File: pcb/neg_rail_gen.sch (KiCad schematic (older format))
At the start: 24 parts, among them U5 LM2596S-ADJ

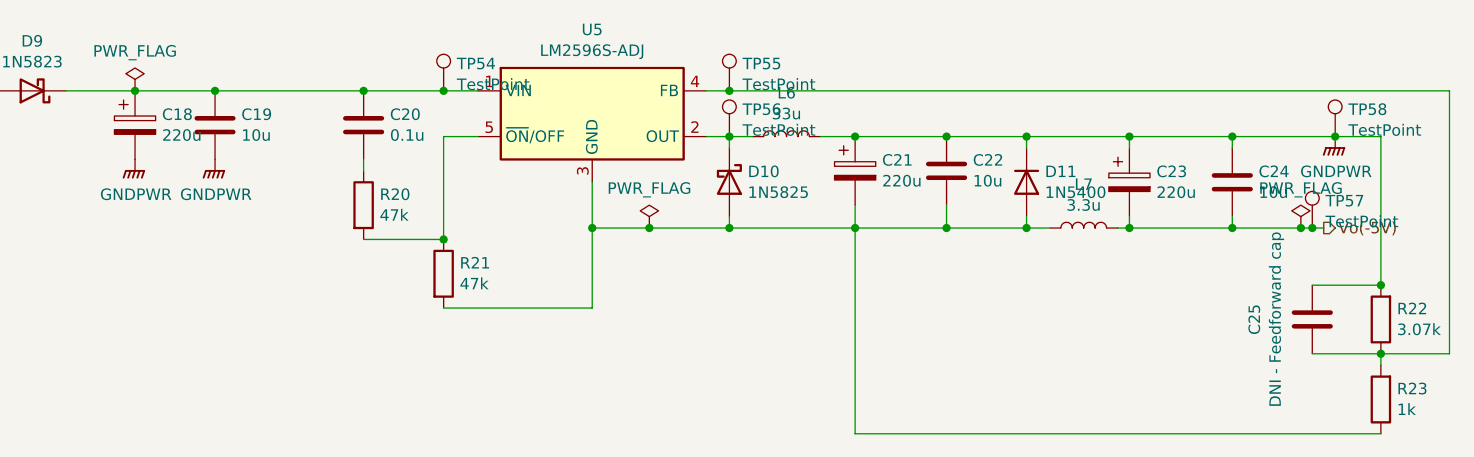
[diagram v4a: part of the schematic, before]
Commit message: Update footprints, move to 0603 passives for JLCPCB assembly, create transformer footprints
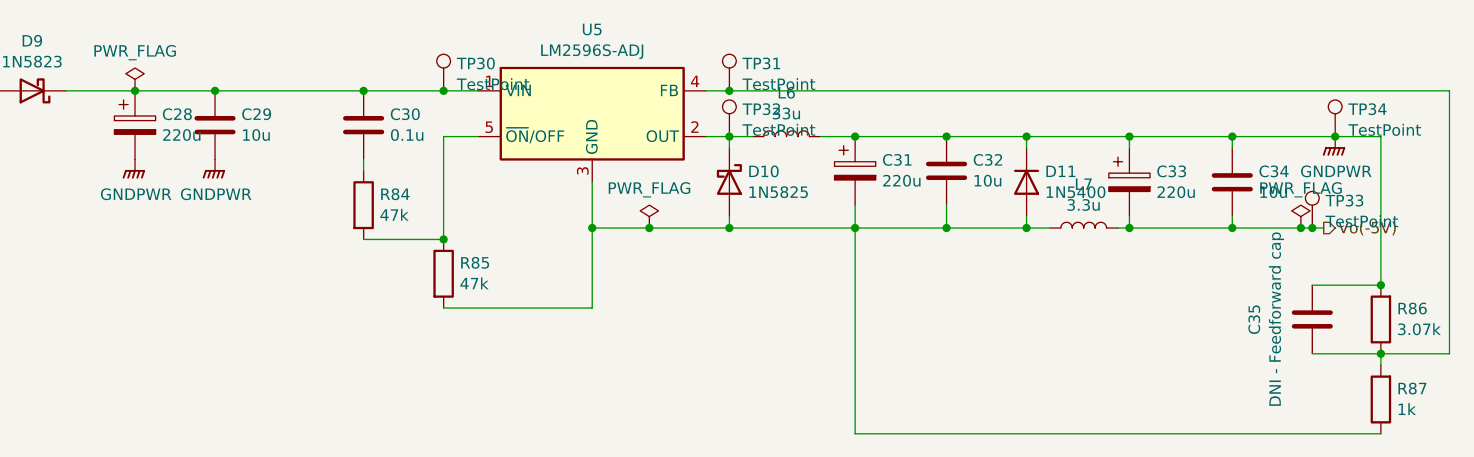
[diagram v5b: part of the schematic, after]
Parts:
- C29: renamed from C19; footprint Capacitor_SMD:C_0805_2012Metric_Pad1.15x1.40mm_HandSolder -> Capacitor_SMD:C_0603_1608Metric
- C30: renamed from C20; footprint Capacitor_SMD:C_0805_2012Metric_Pad1.15x1.40mm_HandSolder -> Capacitor_SMD:C_0603_1608Metric
- C32: renamed from C22; footprint Capacitor_SMD:C_0805_2012Metric_Pad1.15x1.40mm_HandSolder -> Capacitor_SMD:C_0603_1608Metric
- C34: renamed from C24; footprint Capacitor_SMD:C_0805_2012Metric_Pad1.15x1.40mm_HandSolder -> Capacitor_SMD:C_0603_1608Metric
- L6: footprint (none) -> Inductor_SMD:L_Bourns_SRR1260
- L7: footprint (none) -> Inductor_THT:L_Axial_L9.5mm_D4.0mm_P12.70mm_Horizontal_Fastron_SMCC
- R84: renamed from R20; footprint Resistor_SMD:R_0805_2012Metric_Pad1.20x1.40mm_HandSolder -> Resistor_SMD:R_0603_1608Metric
- R85: renamed from R21; footprint Resistor_SMD:R_0805_2012Metric_Pad1.20x1.40mm_HandSolder -> Resistor_SMD:R_0603_1608Metric
- R86: renamed from R22; footprint Resistor_SMD:R_0805_2012Metric_Pad1.20x1.40mm_HandSolder -> Resistor_SMD:R_0603_1608Metric
- R87: renamed from R23; footprint Resistor_SMD:R_0805_2012Metric_Pad1.20x1.40mm_HandSolder -> Resistor_SMD:R_0603_1608Metric
- TP30: renamed from TP54; footprint (none) -> TestPoint:TestPoint_Pad_D1.5mm
- TP31: renamed from TP55; footprint (none) -> TestPoint:TestPoint_Pad_D1.5mm
- TP32: renamed from TP56; footprint (none) -> TestPoint:TestPoint_Pad_D1.5mm
- TP33: renamed from TP57; footprint (none) -> TestPoint:TestPoint_Pad_D1.5mm
- TP34: renamed from TP58; footprint (none) -> TestPoint:TestPoint_Pad_D1.5mm
- renumbered C18 to C28, C21 to C31, C23 to C33, C25 to C35
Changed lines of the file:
@@
 F 0 "L6" V 6840 3600 50  0000 C CNN
 F 1 "33u" V 6749 3600 50  0000 C CNN
-F 2 "" H 6650 3600 50  0001 C CNN
+F 2 "Inductor_SMD:L_Bourns_SRR1260" H 6650 3600 50  0001 C CNN
 F 3 "~" H 6650 3600 50  0001 C CNN
 	1    6650 3600
@@
 	6300 3600 6400 3600
 $Comp
-L Device:CP C21
+L Device:CP C31
 U 1 1 5FD71007
 P 6950 3750
-F 0 "C21" H 7068 3796 50  0000 L CNN
+F 0 "C31" H 7068 3796 50  0000 L CNN
 F 1 "220u" H 7068 3705 50  0000 L CNN
 F 2 "Capacitor_Tantalum_SMD:CP_EIA-7343-20_Kemet-V_Pad2.25x2.55mm_HandSolder" H 6988 3600 50  0001 C CNN
@@
 $EndComp
 $Comp
-L Device:C C22
+L Device:C C32
 U 1 1 5FD73530
 P 7350 3750
-F 0 "C22" H 7235 3704 50  0000 R CNN
+F 0 "C32" H 7235 3704 50  0000 R CNN
 F 1 "10u" H 7235 3795 50  0000 R CNN
-F 2 "Capacitor_SMD:C_0805_2012Metric_Pad1.15x1.40mm_HandSolder" H 7388 3600 50  0001 C CNN
+F 2 "Capacitor_SMD:C_0603_1608Metric" H 7388 3600 50  0001 C CNN
 F 3 "~" H 7350 3750 50  0001 C CNN
 	1    7350 3750
@@
 F 0 "L7" V 8140 4000 50  0000 C CNN
 F 1 "3.3u" V 8049 4000 50  0000 C CNN
-F 2 "" H 7950 4000 50  0001 C CNN
+F 2 "Inductor_THT:L_Axial_L9.5mm_D4.0mm_P12.70mm_Horizontal_Fastron_SMCC" H 7950 4000 50  0001 C CNN
 F 3 "~" H 7950 4000 50  0001 C CNN
 	1    7950 4000
@@
 Connection ~ 8150 3600
 $Comp
-L Device:C C24
+L Device:C C34
 U 1 1 5FD79EE0
 P 8600 3800
-F 0 "C24" H 8485 3754 50  0000 R CNN
+F 0 "C34" H 8485 3754 50  0000 R CNN
 F 1 "10u" H 8485 3845 50  0000 R CNN
-F 2 "Capacitor_SMD:C_0805_2012Metric_Pad1.15x1.40mm_HandSolder" H 8638 3650 50  0001 C CNN
+F 2 "Capacitor_SMD:C_0603_1608Metric" H 8638 3650 50  0001 C CNN
 F 3 "~" H 8600 3800 50  0001 C CNN
 	1    8600 3800
@@
 	6400 3600 6500 3600
 $Comp
-L Device:CP C18
+L Device:CP C28
 U 1 1 5FD8CD2C
 P 3800 3550
-F 0 "C18" H 3918 3596 50  0000 L CNN
+F 0 "C28" H 3918 3596 50  0000 L CNN
 F 1 "220u" H 3918 3505 50  0000 L CNN
 F 2 "Capacitor_Tantalum_SMD:CP_EIA-7343-20_Kemet-V_Pad2.25x2.55mm_HandSolder" H 3838 3400 50  0001 C CNN
@@
 $EndComp
 $Comp
-L power:GNDPWR #PWR0139
+L power:GNDPWR #PWR069
 U 1 1 5FD8CD32
 P 4150 3700
-F 0 "#PWR0139" H 4150 3500 50  0001 C CNN
+F 0 "#PWR069" H 4150 3500 50  0001 C CNN
 F 1 "GNDPWR" H 4154 3546 50  0000 C CNN
 F 2 "" H 4150 3650 50  0001 C CNN
@@
 $EndComp
 $Comp
-L power:GNDPWR #PWR0140
+L power:GNDPWR #PWR068
 U 1 1 5FD8CD38
 P 3800 3700
-F 0 "#PWR0140" H 3800 3500 50  0001 C CNN
+F 0 "#PWR068" H 3800 3500 50  0001 C CNN
 F 1 "GNDPWR" H 3804 3546 50  0000 C CNN
 F 2 "" H 3800 3650 50  0001 C CNN
@@
 $EndComp
 $Comp
-L Device:C C19
+L Device:C C29
 U 1 1 5FD8CD3E
 P 4150 3550
-F 0 "C19" H 4265 3596 50  0000 L CNN
+F 0 "C29" H 4265 3596 50  0000 L CNN
 F 1 "10u" H 4265 3505 50  0000 L CNN
-F 2 "Capacitor_SMD:C_0805_2012Metric_Pad1.15x1.40mm_HandSolder" H 4188 3400 50  0001 C CNN
+F 2 "Capacitor_SMD:C_0603_1608Metric" H 4188 3400 50  0001 C CNN
 F 3 "~" H 4150 3550 50  0001 C CNN
 	1    4150 3550
@@
 Connection ~ 8600 4000
 $Comp
-L Device:CP C23
+L Device:CP C33
 U 1 1 5FDC37D7
 P 8150 3800
-F 0 "C23" H 8268 3846 50  0000 L CNN
+F 0 "C33" H 8268 3846 50  0000 L CNN
 F 1 "220u" H 8268 3755 50  0000 L CNN
 F 2 "Capacitor_Tantalum_SMD:CP_EIA-7343-20_Kemet-V_Pad2.25x2.55mm_HandSolder" H 8188 3650 50  0001 C CNN
@@
 	8100 4000 8150 4000
 $Comp
-L power:GNDPWR #PWR0141
+L power:GNDPWR #PWR070
 U 1 1 5FDC93D0
 P 9050 3600
-F 0 "#PWR0141" H 9050 3400 50  0001 C CNN
+F 0 "#PWR070" H 9050 3400 50  0001 C CNN
 F 1 "GNDPWR" H 9054 3446 50  0000 C CNN
 F 2 "" H 9050 3550 50  0001 C CNN
@@
 	7700 4000 7800 4000
 $Comp
-L Device:R R21
+L Device:R R85
 U 1 1 5FDDC2C2
 P 5150 4200
-F 0 "R21" H 5220 4246 50  0000 L CNN
+F 0 "R85" H 5220 4246 50  0000 L CNN
 F 1 "47k" H 5220 4155 50  0000 L CNN
-F 2 "Resistor_SMD:R_0805_2012Metric_Pad1.20x1.40mm_HandSolder" V 5080 4200 50  0001 C CNN
+F 2 "Resistor_SMD:R_0603_1608Metric" V 5080 4200 50  0001 C CNN
 F 3 "~" H 5150 4200 50  0001 C CNN
 	1    5150 4200
@@
 $EndComp
 $Comp
-L Device:R R20
+L Device:R R84
 U 1 1 5FDDC644
 P 4800 3900
-F 0 "R20" H 4870 3946 50  0000 L CNN
+F 0 "R84" H 4870 3946 50  0000 L CNN
 F 1 "47k" H 4870 3855 50  0000 L CNN
-F 2 "Resistor_SMD:R_0805_2012Metric_Pad1.20x1.40mm_HandSolder" V 4730 3900 50  0001 C CNN
+F 2 "Resistor_SMD:R_0603_1608Metric" V 4730 3900 50  0001 C CNN
 F 3 "~" H 4800 3900 50  0001 C CNN
 	1    4800 3900
@@
 Connection ~ 5800 4000
 $Comp
-L Device:C C20
+L Device:C C30
 U 1 1 5FDEA8C9
 P 4800 3550
-F 0 "C20" H 4915 3596 50  0000 L CNN
+F 0 "C30" H 4915 3596 50  0000 L CNN
 F 1 "0.1u" H 4915 3505 50  0000 L CNN
-F 2 "Capacitor_SMD:C_0805_2012Metric_Pad1.15x1.40mm_HandSolder" H 4838 3400 50  0001 C CNN
+F 2 "Capacitor_SMD:C_0603_1608Metric" H 4838 3400 50  0001 C CNN
 F 3 "~" H 4800 3550 50  0001 C CNN
 	1    4800 3550
@@
 	6950 3600 7350 3600
 $Comp
-L Device:C C25
+L Device:C C35
 U 1 1 5FE0D49B
 P 8950 4400
-F 0 "C25" V 9202 4400 50  0000 C CNN
+F 0 "C35" V 9202 4400 50  0000 C CNN
 F 1 "DNI - Feedforward cap" V 9111 4400 50  0000 C CNN
 F 2 "Capacitor_SMD:C_0805_2012Metric_Pad1.15x1.40mm_HandSolder" H 8988 4250 50  0001 C CNN
@@
 $EndComp
 $Comp
-L Device:R R22
+L Device:R R86
 U 1 1 5FE19832
 P 9250 4400
-F 0 "R22" H 9180 4354 50  0000 R CNN
+F 0 "R86" H 9180 4354 50  0000 R CNN
 F 1 "3.07k" H 9180 4445 50  0000 R CNN
-F 2 "Resistor_SMD:R_0805_2012Metric_Pad1.20x1.40mm_HandSolder" V 9180 4400 50  0001 C CNN
+F 2 "Resistor_SMD:R_0603_1608Metric" V 9180 4400 50  0001 C CNN
 F 3 "~" H 9250 4400 50  0001 C CNN
 	1    9250 4400
@@
 	6950 4900 9250 4900
 $Comp
-L Device:R R23
+L Device:R R87
 U 1 1 5FE1B1CA
 P 9250 4750
-F 0 "R23" H 9180 4704 50  0000 R CNN
+F 0 "R87" H 9180 4704 50  0000 R CNN
 F 1 "1k" H 9180 4795 50  0000 R CNN
-F 2 "Resistor_SMD:R_0805_2012Metric_Pad1.20x1.40mm_HandSolder" V 9180 4750 50  0001 C CNN
+F 2 "Resistor_SMD:R_0603_1608Metric" V 9180 4750 50  0001 C CNN
 F 3 "~" H 9250 4750 50  0001 C CNN
 	1    9250 4750
@@
 	8950 4550 9250 4550
 $Comp
-L power:PWR_FLAG #FLG0102
+L power:PWR_FLAG #FLG07
 U 1 1 5FE36453
 P 8900 4000
-F 0 "#FLG0102" H 8900 4075 50  0001 C CNN
+F 0 "#FLG07" H 8900 4075 50  0001 C CNN
 F 1 "PWR_FLAG" H 8900 4173 50  0000 C CNN
 F 2 "" H 8900 4000 50  0001 C CNN
@@
 	2450 3400 2750 3400
 $Comp
-L power:PWR_FLAG #FLG0104
+L power:PWR_FLAG #FLG05
 U 1 1 5FE3E0B5
 P 3800 3400
-F 0 "#FLG0104" H 3800 3475 50  0001 C CNN
+F 0 "#FLG05" H 3800 3475 50  0001 C CNN
 F 1 "PWR_FLAG" H 3800 3573 50  0000 C CNN
 F 2 "" H 3800 3400 50  0001 C CNN
@@
 $EndComp
 $Comp
-L power:PWR_FLAG #FLG0105
+L power:PWR_FLAG #FLG06
 U 1 1 5FE3F4DD
 P 6050 4000
-F 0 "#FLG0105" H 6050 4075 50  0001 C CNN
+F 0 "#FLG06" H 6050 4075 50  0001 C CNN
 F 1 "PWR_FLAG" H 6050 4173 50  0000 C CNN
 F 2 "" H 6050 4000 50  0001 C CNN
@@
 	6050 4000 6400 4000
 $Comp
-L Connector:TestPoint TP54
+L Connector:TestPoint TP30
 U 1 1 609BE548
 P 5150 3400
-F 0 "TP54" H 5208 3518 50  0000 L CNN
+F 0 "TP30" H 5208 3518 50  0000 L CNN
 F 1 "TestPoint" H 5208 3427 50  0000 L CNN
-F 2 "" H 5350 3400 50  0001 C CNN
+F 2 "TestPoint:TestPoint_Pad_D1.5mm" H 5350 3400 50  0001 C CNN
 F 3 "~" H 5350 3400 50  0001 C CNN
 	1    5150 3400
@@
 	5150 3400 4800 3400
 $Comp
-L Connector:TestPoint TP55
+L Connector:TestPoint TP31
 U 1 1 609BF7FB
 P 6400 3400
-F 0 "TP55" H 6458 3518 50  0000 L CNN
+F 0 "TP31" H 6458 3518 50  0000 L CNN
 F 1 "TestPoint" H 6458 3427 50  0000 L CNN
-F 2 "" H 6600 3400 50  0001 C CNN
+F 2 "TestPoint:TestPoint_Pad_D1.5mm" H 6600 3400 50  0001 C CNN
 F 3 "~" H 6600 3400 50  0001 C CNN
 	1    6400 3400
@@
 	6400 3400 9550 3400
 $Comp
-L Connector:TestPoint TP56
+L Connector:TestPoint TP32
 U 1 1 609C01D4
 P 6400 3600
-F 0 "TP56" H 6458 3718 50  0000 L CNN
+F 0 "TP32" H 6458 3718 50  0000 L CNN
 F 1 "TestPoint" H 6458 3627 50  0000 L CNN
-F 2 "" H 6600 3600 50  0001 C CNN
+F 2 "TestPoint:TestPoint_Pad_D1.5mm" H 6600 3600 50  0001 C CNN
 F 3 "~" H 6600 3600 50  0001 C CNN
 	1    6400 3600
@@
 $EndComp
 $Comp
-L Connector:TestPoint TP57
+L Connector:TestPoint TP33
 U 1 1 609C0F52
 P 8950 4000
-F 0 "TP57" H 9008 4118 50  0000 L CNN
+F 0 "TP33" H 9008 4118 50  0000 L CNN
 F 1 "TestPoint" H 9008 4027 50  0000 L CNN
-F 2 "" H 9150 4000 50  0001 C CNN
+F 2 "TestPoint:TestPoint_Pad_D1.5mm" H 9150 4000 50  0001 C CNN
 F 3 "~" H 9150 4000 50  0001 C CNN
 	1    8950 4000
@@
 	8950 4000 9000 4000
 $Comp
-L Connector:TestPoint TP58
+L Connector:TestPoint TP34
 U 1 1 609C48B5
 P 9050 3600
-F 0 "TP58" H 9108 3718 50  0000 L CNN
+F 0 "TP34" H 9108 3718 50  0000 L CNN
 F 1 "TestPoint" H 9108 3627 50  0000 L CNN
-F 2 "" H 9250 3600 50  0001 C CNN
+F 2 "TestPoint:TestPoint_Pad_D1.5mm" H 9250 3600 50  0001 C CNN
 F 3 "~" H 9250 3600 50  0001 C CNN
 	1    9050 3600

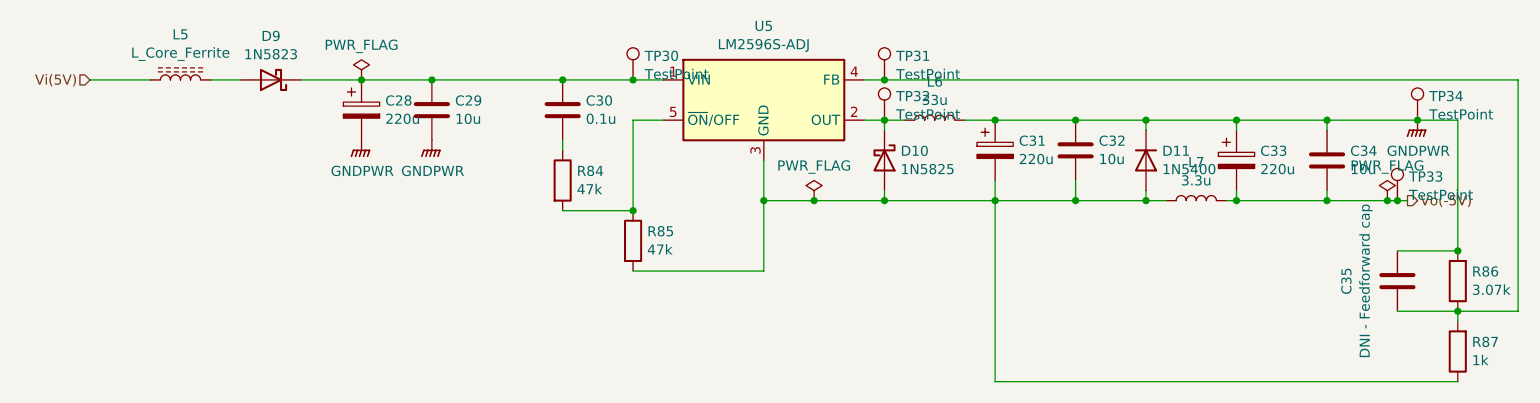
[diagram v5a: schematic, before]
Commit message: finish up vregs, routed filters, iq baseband outputs
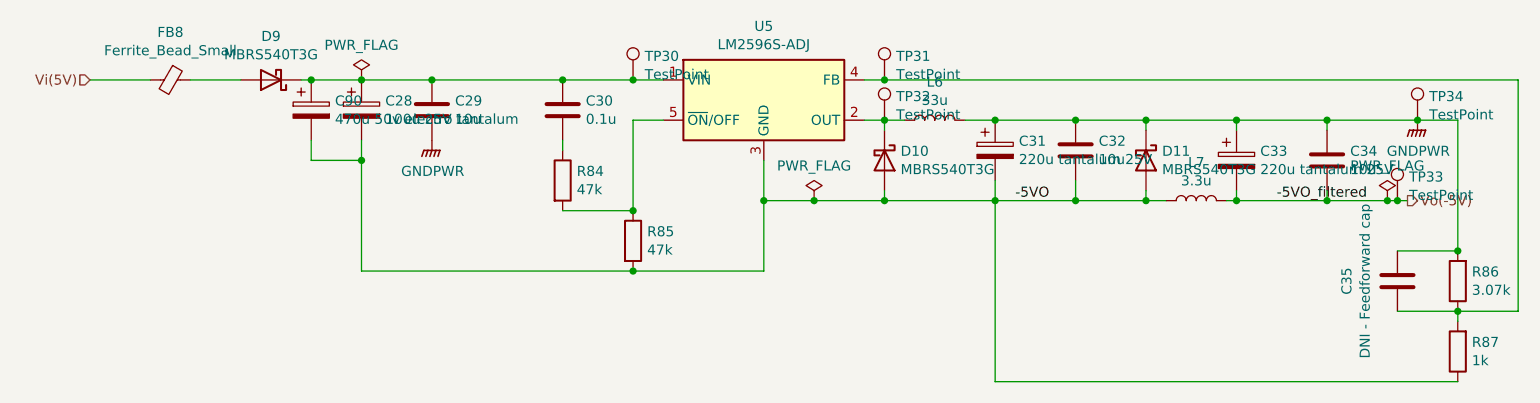
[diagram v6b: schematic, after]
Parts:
- removed D11: 1N5400, Diode_THT:D_DO-201AD_P15.24mm_Horizontal, symbol Diode:1N5400
- removed L5: L_Core_Ferrite, symbol Device:L_Core_Ferrite
- added C90: 470u 50v electro, Capacitor_THT:C_Radial_D10.0mm_H20.0mm_P5.00mm, symbol Device:CP
- added D11: MBRS540T3G, Diode_SMD:D_SMB_Handsoldering, symbol Diode:1N5822
- added FB8: Ferrite_Bead_Small, Inductor_SMD:L_0805_2012Metric_Pad1.05x1.20mm_HandSolder, symbol Device:Ferrite_Bead_Small
- C28: value 220u -> 100u 25V tantalum
- C31, C33: value 220u -> 220u tantalum 25V
- D10: value 1N5825 -> MBRS540T3G; footprint Diode_THT:D_DO-201AD_P15.24mm_Horizontal -> Diode_SMD:D_SMB_Handsoldering
- D9: value 1N5823 -> MBRS540T3G; footprint Diode_THT:D_DO-201AD_P15.24mm_Horizontal -> Diode_SMD:D_SMB_Handsoldering
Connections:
- net GNDPWR: now also D11.1 (K); no longer C28.2
- net Vi(5V): now also FB8.2
- net at C28.1, C29.1, C30.1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: now also C90.1
- net -5VO: now reaches C31.2, C32.1, D10.2 (A), L7.1, R85.2, R87.1, U5.3 (GND)
- net -5VO: now also C28.2, C90.2, D11.2 (A)
- net at D9.2 (A): now also FB8.1
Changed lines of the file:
@@
 P 3350 3400
 F 0 "D9" H 3350 3183 50  0000 C CNN
-F 1 "1N5823" H 3350 3274 50  0000 C CNN
-F 2 "Diode_THT:D_DO-201AD_P15.24mm_Horizontal" H 3350 3225 50  0001 C CNN
-F 3 "http://www.vishay.com/docs/88526/1n5820.pdf" H 3350 3400 50  0001 C CNN
+F 1 "MBRS540T3G" H 3350 3274 50  0000 C CNN
+F 2 "Diode_SMD:D_SMB_Handsoldering" H 3350 3225 50  0001 C CNN
+F 3 "https://www.onsemi.com/pub/Collateral/MBRS540T3-D.PDF" H 3350 3400 50  0001 C CNN
 	1    3350 3400
 	-1   0    0    1
@@
 P 6950 3750
 F 0 "C31" H 7068 3796 50  0000 L CNN
-F 1 "220u" H 7068 3705 50  0000 L CNN
+F 1 "220u tantalum 25V" H 7068 3705 50  0000 L CNN
 F 2 "Capacitor_Tantalum_SMD:CP_EIA-7343-20_Kemet-V_Pad2.25x2.55mm_HandSolder" H 6988 3600 50  0001 C CNN
 F 3 "~" H 6950 3750 50  0001 C CNN
@@
 P 6400 3800
 F 0 "D10" V 6354 3880 50  0000 L CNN
-F 1 "1N5825" V 6445 3880 50  0000 L CNN
-F 2 "Diode_THT:D_DO-201AD_P15.24mm_Horizontal" H 6400 3625 50  0001 C CNN
-F 3 "http://www.vishay.com/docs/88526/1n5820.pdf" H 6400 3800 50  0001 C CNN
+F 1 "MBRS540T3G" V 6445 3880 50  0000 L CNN
+F 2 "Diode_SMD:D_SMB_Handsoldering" H 6400 3625 50  0001 C CNN
+F 3 "https://www.onsemi.com/pub/Collateral/MBRS540T3-D.PDF" H 6400 3800 50  0001 C CNN
 	1    6400 3800
 	0    1    1    0
@@
 P 3800 3550
 F 0 "C28" H 3918 3596 50  0000 L CNN
-F 1 "220u" H 3918 3505 50  0000 L CNN
+F 1 "100u 25V tantalum" H 3918 3505 50  0000 L CNN
 F 2 "Capacitor_Tantalum_SMD:CP_EIA-7343-20_Kemet-V_Pad2.25x2.55mm_HandSolder" H 3838 3400 50  0001 C CNN
 F 3 "~" H 3800 3550 50  0001 C CNN
@@
 $EndComp
 $Comp
-L power:GNDPWR #PWR068
-U 1 1 5FD8CD38
-P 3800 3700
-F 0 "#PWR068" H 3800 3500 50  0001 C CNN
-F 1 "GNDPWR" H 3804 3546 50  0000 C CNN
-F 2 "" H 3800 3650 50  0001 C CNN
-F 3 "" H 3800 3650 50  0001 C CNN
-	1    3800 3700
-	1    0    0    -1
-$EndComp
-$Comp
 L Device:C C29
 U 1 1 5FD8CD3E
@@
 	3800 3400 4150 3400
 Connection ~ 4150 3400
-$Comp
-L Device:L_Core_Ferrite L?
-U 1 1 5FD8CD48
-P 2900 3400
-AR Path="/5FD8CD48" Ref="L?"  Part="1"
-AR Path="/5FC35984/5FD8CD48" Ref="L5"  Part="1"
-F 0 "L5" V 3125 3400 50  0000 C CNN
-F 1 "L_Core_Ferrite" V 3034 3400 50  0000 C CNN
-F 2 "" H 2900 3400 50  0001 C CNN
-F 3 "~" H 2900 3400 50  0001 C CNN
-	1    2900 3400
-	0    -1   -1   0
-$EndComp
 Connection ~ 3800 3400
 Wire Wire Line
@@
 P 8150 3800
 F 0 "C33" H 8268 3846 50  0000 L CNN
-F 1 "220u" H 8268 3755 50  0000 L CNN
+F 1 "220u tantalum 25V" H 8268 3755 50  0000 L CNN
 F 2 "Capacitor_Tantalum_SMD:CP_EIA-7343-20_Kemet-V_Pad2.25x2.55mm_HandSolder" H 8188 3650 50  0001 C CNN
 F 3 "~" H 8150 3800 50  0001 C CNN
@@
 Wire Wire Line
 	7350 4000 7700 4000
-$Comp
-L Diode:1N5400 D11
-U 1 1 5FDD5015
-P 7700 3800
-F 0 "D11" V 7654 3880 50  0000 L CNN
-F 1 "1N5400" V 7745 3880 50  0000 L CNN
-F 2 "Diode_THT:D_DO-201AD_P15.24mm_Horizontal" H 7700 3625 50  0001 C CNN
-F 3 "http://www.vishay.com/docs/88516/1n5400.pdf" H 7700 3800 50  0001 C CNN
-	1    7700 3800
-	0    1    1    0
-$EndComp
 Wire Wire Line
 	7700 3650 7700 3600
@@
 	4800 3700 4800 3750
 Wire Wire Line
-	3500 3400 3800 3400
-Wire Wire Line
-	3200 3400 3050 3400
+	3500 3400 3550 3400
 Wire Wire Line
 	4150 3400 4800 3400
@@
 	1    0    0    -1
 $EndComp
+$Comp
+L Device:Ferrite_Bead_Small FB8
+U 1 1 5FBBC313
+P 2850 3400
+F 0 "FB8" V 2613 3400 50  0000 C CNN
+F 1 "Ferrite_Bead_Small" V 2704 3400 50  0000 C CNN
+F 2 "Inductor_SMD:L_0805_2012Metric_Pad1.05x1.20mm_HandSolder" V 2780 3400 50  0001 C CNN
+F 3 "~" H 2850 3400 50  0001 C CNN
+	1    2850 3400
+	0    1    1    0
+$EndComp
+Wire Wire Line
+	2950 3400 3200 3400
+Wire Wire Line
+	3800 3700 3800 3800
+Wire Wire Line
+	3800 4350 5150 4350
+Connection ~ 5150 4350
+$Comp
+L Diode:1N5822 D11
+U 1 1 5FBBE411
+P 7700 3800
+F 0 "D11" V 7654 3880 50  0000 L CNN
+F 1 "MBRS540T3G" V 7745 3880 50  0000 L CNN
+F 2 "Diode_SMD:D_SMB_Handsoldering" H 7700 3625 50  0001 C CNN
+F 3 "https://www.onsemi.com/pub/Collateral/MBRS540T3-D.PDF" H 7700 3800 50  0001 C CNN
+	1    7700 3800
+	0    1    1    0
+$EndComp
+$Comp
+L Device:CP C90
+U 1 1 5FBC18F7
+P 3550 3550
+F 0 "C90" H 3668 3596 50  0000 L CNN
+F 1 "470u 50v electro" H 3668 3505 50  0000 L CNN
+F 2 "Capacitor_THT:C_Radial_D10.0mm_H20.0mm_P5.00mm" H 3588 3400 50  0001 C CNN
+F 3 "~" H 3550 3550 50  0001 C CNN
+	1    3550 3550
+	1    0    0    -1
+$EndComp
+Connection ~ 3550 3400
+Wire Wire Line
+	3550 3400 3800 3400
+Wire Wire Line
+	3550 3700 3550 3800
+Wire Wire Line
+	3550 3800 3800 3800
+Connection ~ 3800 3800
+Wire Wire Line
+	3800 3800 3800 4350
+Text Label 7050 4000 0    50   ~ 0
+-5VO
+Text Label 8350 4000 0    50   ~ 0
+-5VO_filtered
 $EndSCHEMATC

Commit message: layout progress
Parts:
- removed C90: 470u 50v electro, Capacitor_THT:C_Radial_D10.0mm_H20.0mm_P5.00mm, symbol Device:CP
- C28: value 100u 25V tantalum -> 220u 25V tantalum
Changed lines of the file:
@@
 P 3800 3550
 F 0 "C28" H 3918 3596 50  0000 L CNN
-F 1 "100u 25V tantalum" H 3918 3505 50  0000 L CNN
+F 1 "220u 25V tantalum" H 3918 3505 50  0000 L CNN
 F 2 "Capacitor_Tantalum_SMD:CP_EIA-7343-20_Kemet-V_Pad2.25x2.55mm_HandSolder" H 3838 3400 50  0001 C CNN
 F 3 "~" H 3800 3550 50  0001 C CNN
@@
 Wire Wire Line
 	4800 3700 4800 3750
-Wire Wire Line
-	3500 3400 3550 3400
 Wire Wire Line
 	4150 3400 4800 3400
@@
 	2950 3400 3200 3400
 Wire Wire Line
-	3800 3700 3800 3800
-Wire Wire Line
 	3800 4350 5150 4350
 Connection ~ 5150 4350
@@
 	0    1    1    0
 $EndComp
-$Comp
-L Device:CP C90
-U 1 1 5FBC18F7
-P 3550 3550
-F 0 "C90" H 3668 3596 50  0000 L CNN
-F 1 "470u 50v electro" H 3668 3505 50  0000 L CNN
-F 2 "Capacitor_THT:C_Radial_D10.0mm_H20.0mm_P5.00mm" H 3588 3400 50  0001 C CNN
-F 3 "~" H 3550 3550 50  0001 C CNN
-	1    3550 3550
-	1    0    0    -1
-$EndComp
-Connection ~ 3550 3400
-Wire Wire Line
-	3550 3400 3800 3400
-Wire Wire Line
-	3550 3700 3550 3800
-Wire Wire Line
-	3550 3800 3800 3800
-Connection ~ 3800 3800
-Wire Wire Line
-	3800 3800 3800 4350
 Text Label 7050 4000 0    50   ~ 0
 -5VO
 Text Label 8350 4000 0    50   ~ 0
 -5VO_filtered
+Wire Wire Line
+	3500 3400 3800 3400
+Wire Wire Line
+	3800 3700 3800 4350
 $EndSCHEMATC
